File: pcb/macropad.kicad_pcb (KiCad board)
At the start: 2 copper layers, 104.1 x 141 mm, 23 parts, among them SW1 RotaryEncoder_Switch, SW10 SW_Push, SW2 SW_Push, SW3 SW_Push, SW4 SW_Push, SW5 SW_Push, SW6 SW_Push, SW7 SW_Push, SW8 SW_Push, SW9 SW_Push, U1 PICO_RP2040

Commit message: First Possible release
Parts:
- added REF**: MountingHole_2.5mm, MountingHole:MountingHole_2.5mm, F.Cu at (138.4, 158.8)
- added REF**: MountingHole_2.5mm, MountingHole:MountingHole_2.5mm, F.Cu at (43.2, 158.8)
- added REF**: MountingHole_2.5mm, MountingHole:MountingHole_2.5mm, F.Cu at (45.7, 27.9)
- added REF**: MountingHole_2.5mm, MountingHole:MountingHole_2.5mm, F.Cu at (138.4, 29.2)
- moved D5 6.54 mm to (80.6, 119.3)
- moved D6 6.54 mm to (80.6, 144.8)
- moved D8 6.54 mm to (107.3, 119.3)
- moved D9 6.54 mm to (107.3, 144.8)
- moved R1 6.54 mm to (70.5, 154.0)
- moved R2 6.54 mm to (96.5, 154.0)
- moved R3 6.54 mm to (123.2, 154.0)
- moved SW10 6.54 mm to (122.6, 131.4)
- moved SW4 6.54 mm to (70.5, 131.4)
- moved SW7 6.54 mm to (97.2, 131.4)
- moved D2 6.54 mm to (54.0, 119.3)
- moved D3 6.54 mm to (54.0, 144.8)
- moved D7 6.54 mm to (107.3, 95.2)
- moved SW2 6.54 mm to (70.5, 81.9)
- moved SW3 6.54 mm to (70.5, 106.0)
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
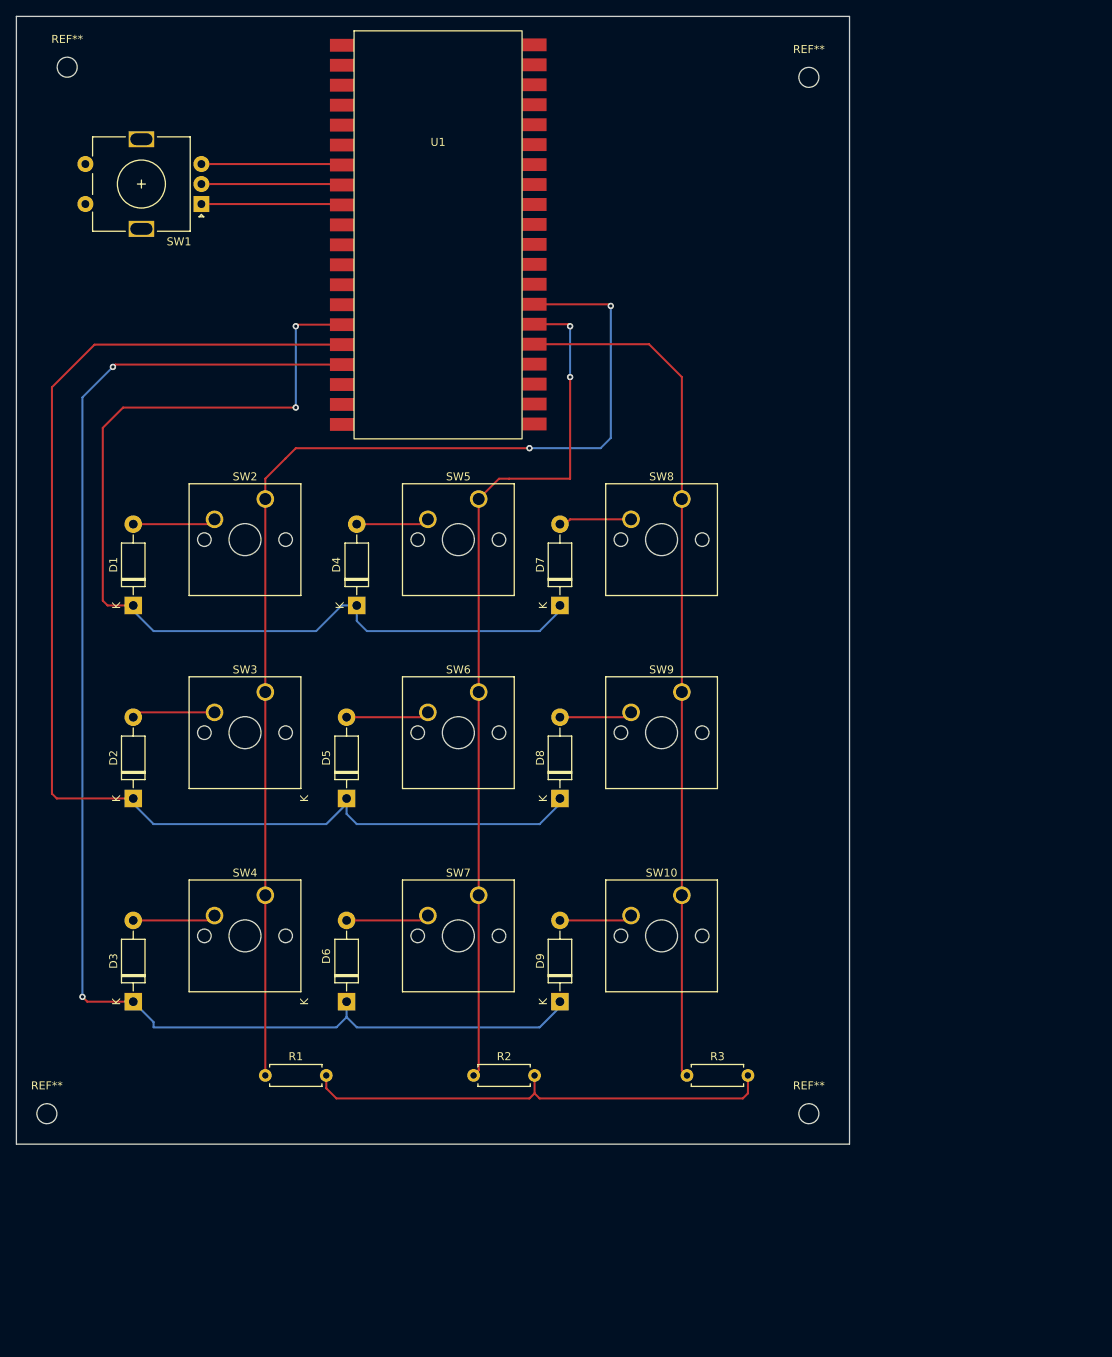
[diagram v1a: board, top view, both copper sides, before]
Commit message: Added leds and connected switch from rotary encoder
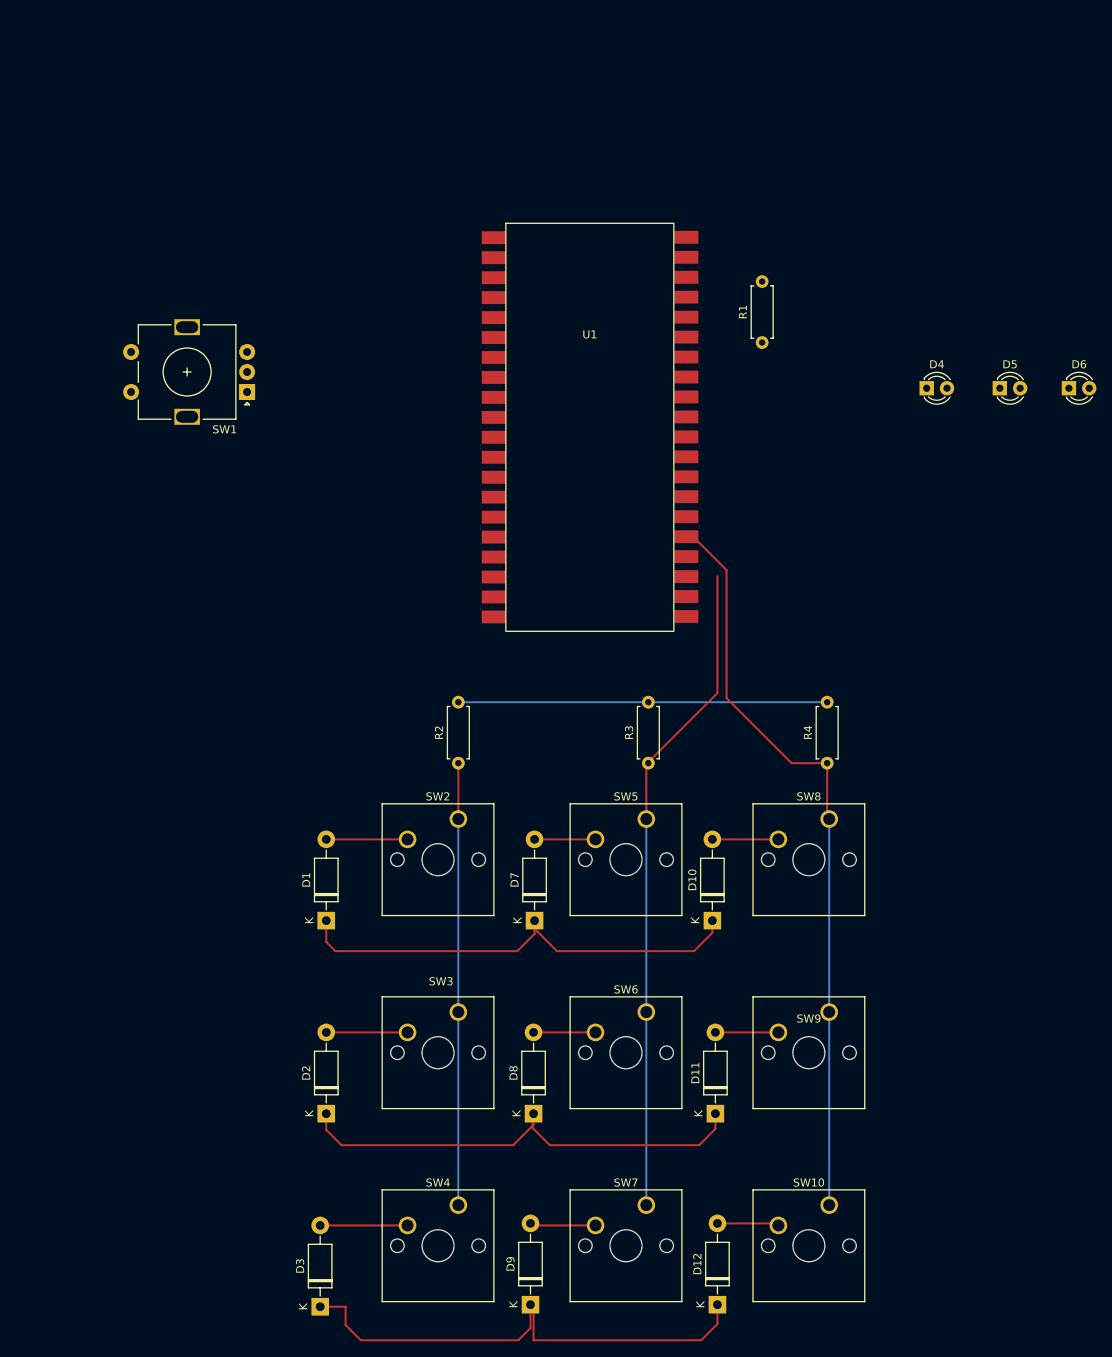
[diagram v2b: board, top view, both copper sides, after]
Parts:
- removed REF** (x4): MountingHole_2.5mm, MountingHole:MountingHole_2.5mm
- added D10: 1N4007, Diode_THT:D_DO-41_SOD81_P10.16mm_Horizontal, F.Cu at (126.4, 134.6)
- added D11: 1N4007, Diode_THT:D_DO-41_SOD81_P10.16mm_Horizontal, F.Cu at (126.7, 158.8)
- added D12: 1N4007, Diode_THT:D_DO-41_SOD81_P10.16mm_Horizontal, F.Cu at (127.0, 182.6)
- added R4: R, Resistor_THT:R_Axial_DIN0207_L6.3mm_D2.5mm_P7.62mm_Horizontal, F.Cu at (140.7, 114.9)
- D4, D5, D6: value 1N4007 -> LED; footprint Diode_THT:D_DO-41_SOD81_P10.16mm_Horizontal -> LED_THT:LED_D3.0mm
- moved D6 118.5 mm to (170.9, 68.1), turned to 0 degrees
- moved R1 110.7 mm to (132.6, 62.4), turned to 90 degrees
- moved D5 96.4 mm to (162.3, 68.1), turned to 0 degrees
- moved D4 76.2 mm to (153.2, 68.1), turned to 0 degrees
- moved SW3 46.7 mm to (94.6, 146.1)
- moved SW2 46.7 mm to (94.6, 121.9)
- moved D1 46.2 mm to (78.1, 134.6)
- moved D2 46.2 mm to (78.1, 158.8)
- moved SW4 45.6 mm to (94.6, 170.2)
- moved SW6 45.2 mm to (118.1, 146.1)
- moved SW5 45.2 mm to (118.1, 121.9)
- moved D3 44.7 mm to (77.3, 182.9)
- moved SW7 44.0 mm to (118.1, 170.2)
- moved SW9 44.0 mm to (141.0, 146.1)
- moved SW8 44.0 mm to (141.0, 121.9)
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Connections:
- D4 pad 1: /Pin 15 -> Net-(D4-Pad1)
- D5 pad 1: /Pin 16 -> Net-(D5-Pad1)
- D5 pad 2: Net-(D5-Pad2) -> Net-(D4-Pad2)
- D6 pad 1: /Pin 17 -> Net-(D6-Pad1)
- D6 pad 2: Net-(D6-Pad2) -> Net-(D4-Pad2)
- SW1 pad S1: unconnected-(SW1-PadS1) -> Net-(SW1-PadS1)
- SW1 pad S2: unconnected-(SW1-PadS2) -> Net-(SW1-PadS2)
- SW10 pad 1: Net-(R3-Pad1) -> Net-(R4-Pad1)
- SW10 pad 2: Net-(D9-Pad2) -> Net-(D12-Pad2)
- SW2 pad 1: Net-(R1-Pad1) -> Net-(R2-Pad1)
- SW3 pad 1: Net-(R1-Pad1) -> Net-(R2-Pad1)
- SW4 pad 1: Net-(R1-Pad1) -> Net-(R2-Pad1)
- SW5 pad 1: Net-(R2-Pad1) -> Net-(R3-Pad1)
- SW5 pad 2: Net-(D4-Pad2) -> Net-(D7-Pad2)
- SW6 pad 1: Net-(R2-Pad1) -> Net-(R3-Pad1)
- SW6 pad 2: Net-(D5-Pad2) -> Net-(D8-Pad2)
- SW7 pad 1: Net-(R2-Pad1) -> Net-(R3-Pad1)
- SW7 pad 2: Net-(D6-Pad2) -> Net-(D9-Pad2)
- SW8 pad 1: Net-(R3-Pad1) -> Net-(R4-Pad1)
- SW8 pad 2: Net-(D7-Pad2) -> Net-(D10-Pad2)
- SW9 pad 1: Net-(R3-Pad1) -> Net-(R4-Pad1)
- SW9 pad 2: Net-(D8-Pad2) -> Net-(D11-Pad2)
- U1 pad 11: unconnected-(U1-Pad11) -> Net-(SW1-PadS1)
- U1 pad 25: Net-(R3-Pad1) -> Net-(R4-Pad1)
- U1 pad 26: Net-(R2-Pad1) -> Net-(R3-Pad1)
- U1 pad 27: Net-(R1-Pad1) -> Net-(R2-Pad1)
- U1 pad 3: unconnected-(U1-Pad3) -> Net-(SW1-PadS2)
- U1 pad 31: unconnected-(U1-Pad31) -> Net-(D6-Pad1)
- U1 pad 32: unconnected-(U1-Pad32) -> Net-(D5-Pad1)
- U1 pad 34: unconnected-(U1-Pad34) -> Net-(D4-Pad1)
- U1 pad 38: unconnected-(U1-Pad38) -> Net-(R1-Pad2)
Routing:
- net Net-(R1-Pad1): track 146.0 -> 0.00 mm, vias 2 -> 0
- net /Pin 17: track 175.4 -> 64.6 mm, vias 2 -> 0
- net /Pin 16: track 160.6 -> 59.5 mm
- net Net-(R4-Pad1): track 0.00 -> 94.4 mm
- net /Pin 15: track 127.4 -> 58.6 mm, vias 2 -> 0
- net Net-(R2-Pad1): track 108.4 -> 55.2 mm, vias 2 -> 0
- net Net-(R3-Pad1): track 107.7 -> 82.4 mm
- net Net-(SW1-PadB): track 18.6 -> 0.00 mm
- net Net-(SW1-PadC): track 17.6 -> 0.00 mm
- net Net-(SW1-PadA): track 17.6 -> 0.00 mm
- net GND: track 60.1 -> 46.1 mm
- net Net-(D5-Pad2): track 10.4 -> 0.00 mm
- net Net-(D6-Pad2): track 10.4 -> 0.00 mm
- net Net-(D4-Pad2): track 9.14 -> 0.00 mm
- net Net-(D10-Pad2): track 0.00 -> 8.26 mm
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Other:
- board outline removed
